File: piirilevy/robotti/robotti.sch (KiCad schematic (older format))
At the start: 63 parts, among them J1 VL53L1X, J2 VL53L1X, J3 XT30, J4 ST-LINK_V2, J5 UART, J6 Nema14, J7 Nema14, Q1 ALS-PT19-315C, SW1 SW_SPST, U1 ICM-42605, U2 STM32F410RBTx, U3 TMP235, U4 RC-SM1276-868, U5 L5973D, Y1 ABL-8.000MHZ-B2

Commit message: PCB V2.0
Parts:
- removed C1: 10nF, Capacitor_SMD:C_0805_2012Metric, symbol Device:C
- removed C2: 0.1uF, Capacitor_SMD:C_0805_2012Metric, symbol Device:C
- removed C3: 2.2uF, Capacitor_SMD:C_0805_2012Metric, symbol Device:C
- removed U1: ICM-42605, Package_LGA:LGA-14_3x2.5mm_P0.5mm_LayoutBorder3x4y, symbol robotti_library:ICM-42605
- added U1: SEN0373, robotti:PinHeader_1x07_PinHeader_SEN0373, symbol robotti_library:SEN0373
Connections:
- net GND: now also U1.2 (GND)
- net PA2: no longer J5.1 (TX)
- net PA3: no longer J5.2 (RX)
- net PA9: no longer JP2.8 (En/CFG6)
- net PB10: now also J1.5 (SCL); no longer J2.5 (SCL)
- net PB11: now also J1.4 (SDA); no longer J2.4 (SDA)
- net PB12: now also JP1.1 (DIR); no longer U4.15 (NSS)
- net PB14: now also J2.4 (SDA); no longer U4.13 (MISO)
- net PB15: now also J2.5 (SCL); no longer U4.14 (MOSI)
- net PB6: now also U1.3 (SCL); no longer J1.5 (SCL)
- net PB7: now also U1.4 (SDA); no longer J1.4 (SDA)
- net PB9: now also U4.15 (NSS); no longer U4.6 (DIO0)
- net PC0: no longer R12.2, R13.2
- net PC1: now also R12.2, R13.2; no longer JP1.1 (DIR)
- net PC2: now also U4.13 (MISO); no longer JP1.2 (STEP)
- net PC3: now also U4.14 (MOSI); no longer JP1.8 (En/CFG6)
- net PC7: now also J5.2 (RX)
- net PC8: now also JP1.8 (En/CFG6)
- net VDD: now also U1.1 (VCC)
- net PC14: now reaches Q1.2 (E), R6.1
- net PC14: now also U2.3 (PC14); no longer U2.14 (PA0)
- net PC13: now reaches C11.1, U3.2 (Vout)
- net PC13: now also U2.2 (PC13); no longer U2.15 (PA1)
- net PA15: now reaches R3.1
- net PA15: now also U2.50 (PA15); no longer U2.2 (PC13)
- net PB2: now reaches U2.28 (PB2)
- net PB2: now also JP2.8 (En/CFG6)
- net PC6: now reaches U2.37 (PC6)
- net PC6: now also JP1.2 (STEP)
- net PA11: now reaches U2.44 (PA11)
- net PA11: now also J5.1 (TX)
- net at U2.51 (PC10): now also R2.1
- net PC12: now reaches U2.53 (PC12)
- net PC12: now also U1.7 (INT2); no longer R2.1
- net PB4: now reaches U2.56 (PB4)
- net PB4: now also U1.6 (INT1)
- net PB5: now reaches U2.57 (PB5)
- net PB5: now also U4.6 (DIO0)
- new net PA1: U2.15 (PA1)
- no-connect marks 24 -> 25
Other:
- note added: "I2C1"
- note added: "I2C4"
- note added: "SPI1"
- note added: "SPI2"
- note added: "SPI5"
- moved on the sheet: C11, C13, J5, R7, R8, U3

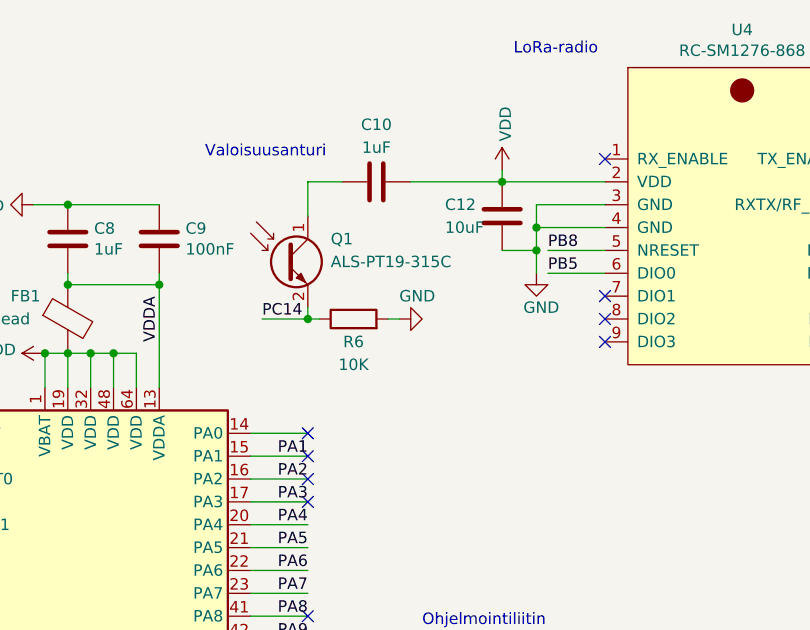
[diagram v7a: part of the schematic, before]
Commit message: Generoitu Platformio IO projekti CubeMX conffista
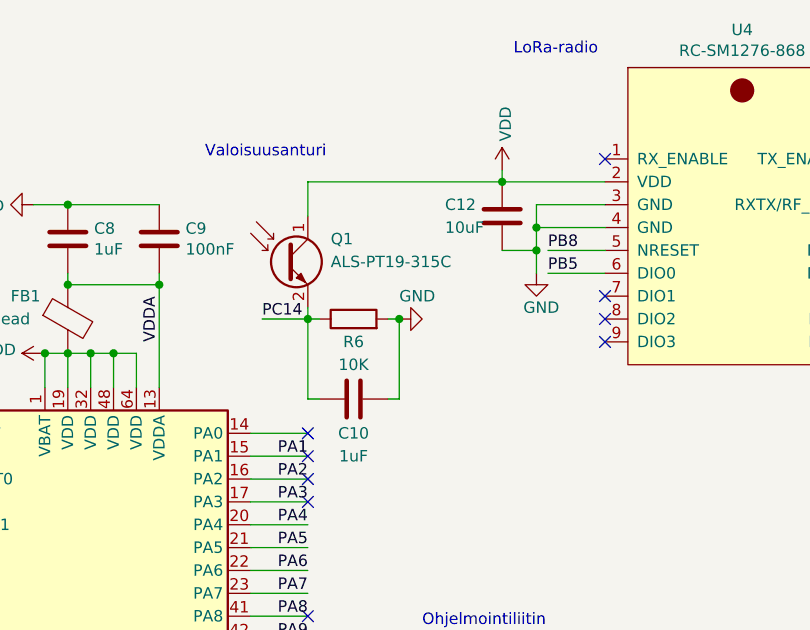
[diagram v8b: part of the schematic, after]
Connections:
- net GND: now also C10.2
- net PC14: now also C10.1
- net VDD: now also Q1.1 (C); no longer C10.2
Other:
- moved on the sheet: C10
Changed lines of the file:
@@
 L Device:C C10
 U 1 1 606750D5
-P 7000 1200
-F 0 "C10" V 7250 1200 50  0000 C CNN
-F 1 "1uF" V 7150 1200 50  0000 C CNN
-F 2 "Capacitor_SMD:C_0805_2012Metric" H 7038 1050 50  0001 C CNN
-F 3 "~" H 7000 1200 50  0001 C CNN
-	1    7000 1200
+P 6900 2150
+F 0 "C10" V 6750 2150 50  0000 C CNN
+F 1 "1uF" V 6650 2150 50  0000 C CNN
+F 2 "Capacitor_SMD:C_0805_2012Metric" H 6938 2000 50  0001 C CNN
+F 3 "~" H 6900 2150 50  0001 C CNN
+	1    6900 2150
 	0    -1   -1   0
 $EndComp
-Wire Wire Line
-	7150 1200 7550 1200
-Wire Wire Line
-	6850 1200 6700 1200
 Wire Wire Line
 	6700 1750 6700 1800
@@
 Wire Wire Line
 	7550 5550 7600 5550
+Wire Wire Line
+	7050 2150 7100 2150
+Wire Wire Line
+	7100 2150 7100 1800
+Connection ~ 7100 1800
+Wire Wire Line
+	6750 2150 6700 2150
+Wire Wire Line
+	6700 2150 6700 1800
+Wire Wire Line
+	6700 1200 7550 1200
 $EndSCHEMATC
